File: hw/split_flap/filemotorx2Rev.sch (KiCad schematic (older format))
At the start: 4 parts, among them J13 Conn_01x05, J14 Conn_01x05, U7 PCF8574, U8 ULN2803A

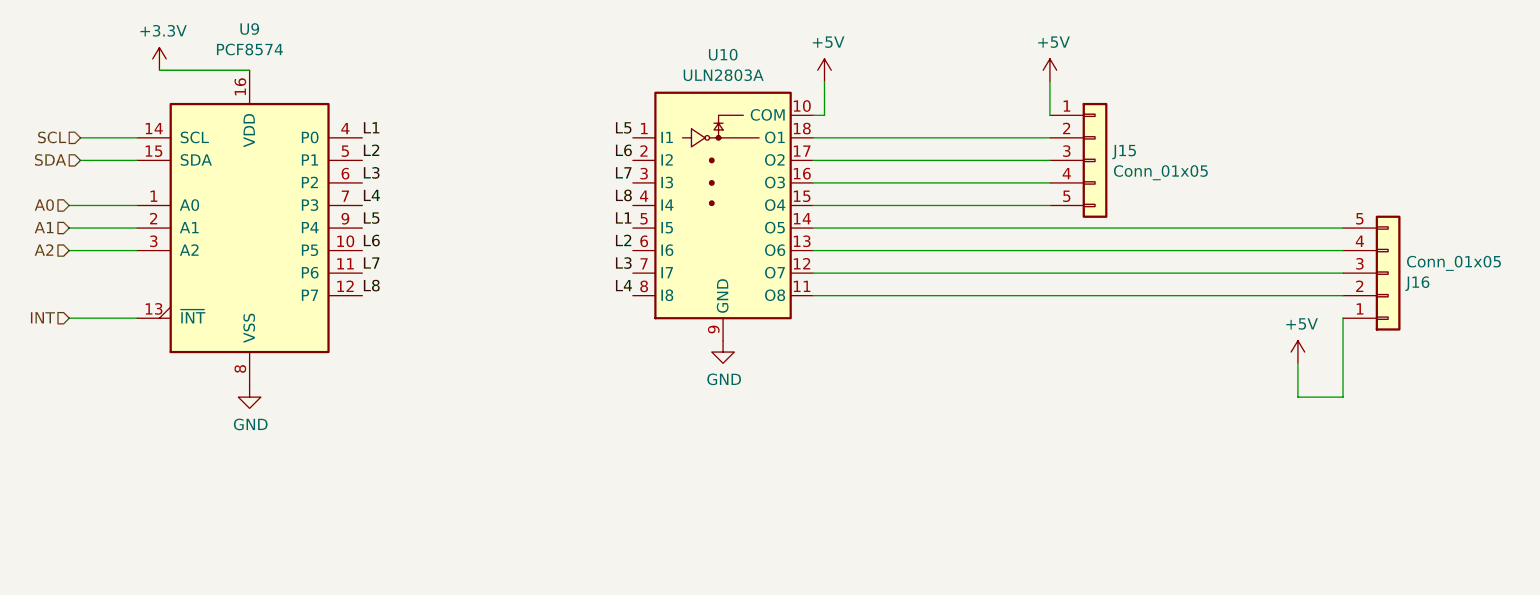
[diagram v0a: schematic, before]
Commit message: Reroute full PCB
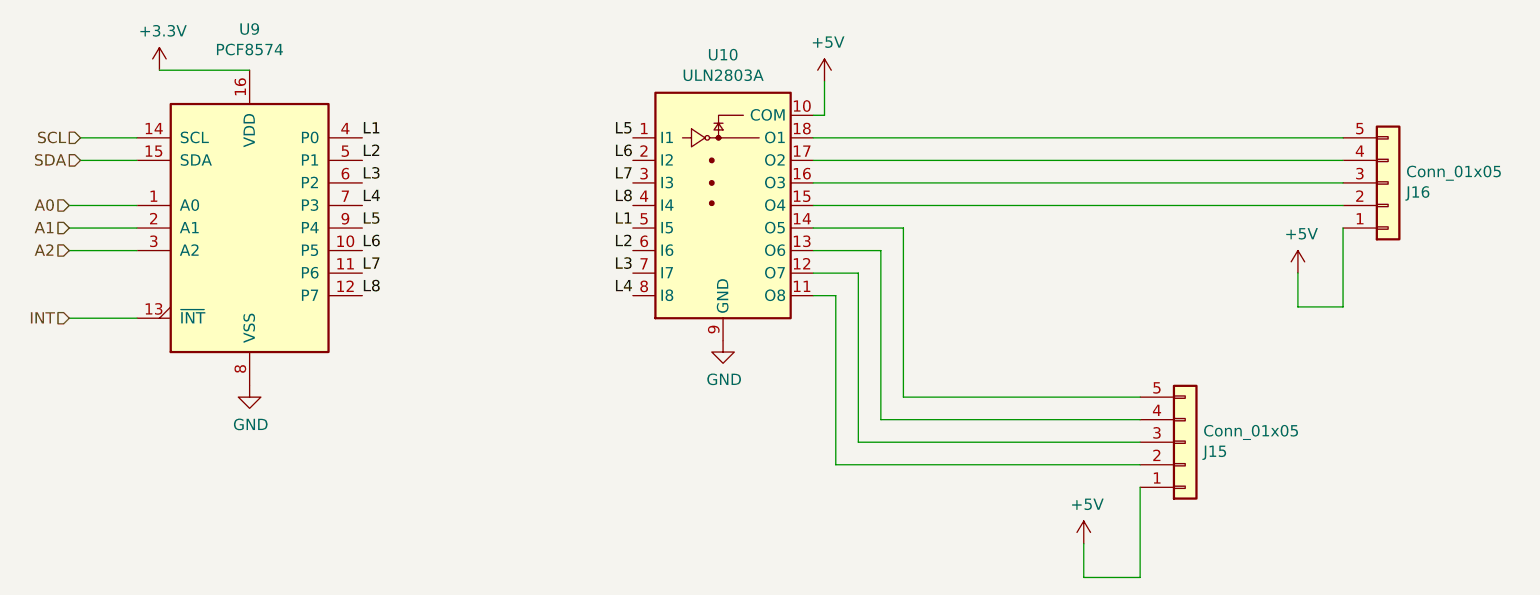
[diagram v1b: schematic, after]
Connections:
- net at J14.2 (Pin_2): now also U8.15 (O4); no longer U8.11 (O8)
- net at J14.3 (Pin_3): now also U8.16 (O3); no longer U8.12 (O7)
- net at J14.4 (Pin_4): now also U8.17 (O2); no longer U8.13 (O6)
- net at J14.5 (Pin_5): now also U8.18 (O1); no longer U8.14 (O5)
- net at J13.2 (Pin_2): now also U8.11 (O8); no longer U8.18 (O1)
- net at J13.3 (Pin_3): now also U8.12 (O7); no longer U8.17 (O2)
- net at J13.4 (Pin_4): now also U8.13 (O6); no longer U8.16 (O3)
- net at J13.5 (Pin_5): now also U8.14 (O5); no longer U8.15 (O4)
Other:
- moved on the sheet: J15, J16
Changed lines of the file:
@@
 $Descr A4 11693 8268
 encoding utf-8
-Sheet 4 7
+Sheet 5 7
 Title ""
 Date ""
@@
 	3400 3200 3000 3200
 Wire Wire Line
-	5900 4200 8250 4200
-Wire Wire Line
-	5900 4100 8250 4100
-Wire Wire Line
-	5900 4000 8250 4000
-Wire Wire Line
-	5900 3900 8250 3900
-Wire Wire Line
-	8050 4500 8050 4650
-$Comp
-L power:+5V #PWR?
-U 1 1 5DE20FD2
-P 8050 4500
-AR Path="/5DE20FD2" Ref="#PWR?"  Part="1"
-AR Path="/5E0CA2EA/5DE20FD2" Ref="#PWR?"  Part="1"
-AR Path="/5E1C4151/5DE20FD2" Ref="#PWR?"  Part="1"
-AR Path="/5E1CE3D2/5DE20FD2" Ref="#PWR?"  Part="1"
-AR Path="/5E1D4C2D/5DE20FD2" Ref="#PWR?"  Part="1"
-AR Path="/5E2ED868/5DE20FD2" Ref="#PWR?"  Part="1"
-AR Path="/5DE1D349/5DE20FD2" Ref="#PWR0121"  Part="1"
-AR Path="/5DE57FF9/5DE20FD2" Ref="#PWR0137"  Part="1"
-F 0 "#PWR0137" H 8050 4350 50  0001 C CNN
-F 1 "+5V" H 8065 4673 50  0000 C CNN
-F 2 "" H 8050 4500 50  0001 C CNN
-F 3 "" H 8050 4500 50  0001 C CNN
-	1    8050 4500
-	1    0    0    -1
-$EndComp
-$Comp
-L Connector_Generic:Conn_01x05 J?
-U 1 1 5DE20FD8
-P 8450 4100
-AR Path="/5DE20FD8" Ref="J?"  Part="1"
-AR Path="/5E0CA2EA/5DE20FD8" Ref="J?"  Part="1"
-AR Path="/5E1C4151/5DE20FD8" Ref="J?"  Part="1"
-AR Path="/5E1CE3D2/5DE20FD8" Ref="J?"  Part="1"
-AR Path="/5E1D4C2D/5DE20FD8" Ref="J?"  Part="1"
-AR Path="/5E2ED868/5DE20FD8" Ref="J?"  Part="1"
-AR Path="/5DE1D349/5DE20FD8" Ref="J14"  Part="1"
-AR Path="/5DE57FF9/5DE20FD8" Ref="J16"  Part="1"
-F 0 "J16" H 8530 4142 50  0000 L CNN
-F 1 "Conn_01x05" H 8530 4051 50  0000 L CNN
-F 2 "Connector_JST:JST_XH_B5B-XH-A_1x05_P2.50mm_Vertical" H 8450 4100 50  0001 C CNN
-F 3 "~" H 8450 4100 50  0001 C CNN
-	1    8450 4100
-	1    0    0    1
-$EndComp
-Wire Wire Line
 	5950 3400 5900 3400
 Wire Wire Line
 	5950 3250 5950 3400
-Wire Wire Line
-	6950 3250 6950 3400
-$Comp
-L power:+5V #PWR?
-U 1 1 5DE20FE1
-P 6950 3250
-AR Path="/5DE20FE1" Ref="#PWR?"  Part="1"
-AR Path="/5E0CA2EA/5DE20FE1" Ref="#PWR?"  Part="1"
-AR Path="/5E1C4151/5DE20FE1" Ref="#PWR?"  Part="1"
-AR Path="/5E1CE3D2/5DE20FE1" Ref="#PWR?"  Part="1"
-AR Path="/5E1D4C2D/5DE20FE1" Ref="#PWR?"  Part="1"
-AR Path="/5E2ED868/5DE20FE1" Ref="#PWR?"  Part="1"
-AR Path="/5DE1D349/5DE20FE1" Ref="#PWR0124"  Part="1"
-AR Path="/5DE57FF9/5DE20FE1" Ref="#PWR0138"  Part="1"
-F 0 "#PWR0138" H 6950 3100 50  0001 C CNN
-F 1 "+5V" H 6965 3423 50  0000 C CNN
-F 2 "" H 6950 3250 50  0001 C CNN
-F 3 "" H 6950 3250 50  0001 C CNN
-	1    6950 3250
-	1    0    0    -1
-$EndComp
 $Comp
 L power:+5V #PWR?
@@
 $EndComp
 $Comp
-L Connector_Generic:Conn_01x05 J?
-U 1 1 5DE20FF9
-P 7150 3600
-AR Path="/5DE20FF9" Ref="J?"  Part="1"
-AR Path="/5E0CA2EA/5DE20FF9" Ref="J?"  Part="1"
-AR Path="/5E1C4151/5DE20FF9" Ref="J?"  Part="1"
-AR Path="/5E1CE3D2/5DE20FF9" Ref="J?"  Part="1"
-AR Path="/5E1D4C2D/5DE20FF9" Ref="J?"  Part="1"
-AR Path="/5E2ED868/5DE20FF9" Ref="J?"  Part="1"
-AR Path="/5DE1D349/5DE20FF9" Ref="J13"  Part="1"
-AR Path="/5DE57FF9/5DE20FF9" Ref="J15"  Part="1"
-F 0 "J15" H 7230 3642 50  0000 L CNN
-F 1 "Conn_01x05" H 7230 3551 50  0000 L CNN
-F 2 "Connector_JST:JST_XH_B5B-XH-A_1x05_P2.50mm_Vertical" H 7150 3600 50  0001 C CNN
-F 3 "~" H 7150 3600 50  0001 C CNN
-	1    7150 3600
-	1    0    0    -1
-$EndComp
-Wire Wire Line
-	6950 3800 5900 3800
-Wire Wire Line
-	5900 3700 6950 3700
-Wire Wire Line
-	6950 3600 5900 3600
-Wire Wire Line
-	5900 3500 6950 3500
-$Comp
 L Interface_Expansion:PCF8574 U?
 U 1 1 5DE21003
@@
 	1    0    0    -1
 $EndComp
-Wire Wire Line
-	8250 4300 8250 4650
-Wire Wire Line
-	8250 4650 8050 4650
 Text Label 3900 3500 0    50   ~ 0
 L1
@@
 Text Label 5100 3800 2    50   ~ 0
 L8
+Wire Wire Line
+	8250 4250 8050 4250
+Wire Wire Line
+	8250 3900 8250 4250
+$Comp
+L Connector_Generic:Conn_01x05 J?
+U 1 1 5DE20FD8
+P 8450 3700
+AR Path="/5DE20FD8" Ref="J?"  Part="1"
+AR Path="/5E0CA2EA/5DE20FD8" Ref="J?"  Part="1"
+AR Path="/5E1C4151/5DE20FD8" Ref="J?"  Part="1"
+AR Path="/5E1CE3D2/5DE20FD8" Ref="J?"  Part="1"
+AR Path="/5E1D4C2D/5DE20FD8" Ref="J?"  Part="1"
+AR Path="/5E2ED868/5DE20FD8" Ref="J?"  Part="1"
+AR Path="/5DE1D349/5DE20FD8" Ref="J14"  Part="1"
+AR Path="/5DE57FF9/5DE20FD8" Ref="J16"  Part="1"
+F 0 "J16" H 8530 3742 50  0000 L CNN
+F 1 "Conn_01x05" H 8530 3651 50  0000 L CNN
+F 2 "Connector_JST:JST_XH_B5B-XH-A_1x05_P2.50mm_Vertical" H 8450 3700 50  0001 C CNN
+F 3 "~" H 8450 3700 50  0001 C CNN
+	1    8450 3700
+	1    0    0    1
+$EndComp
+$Comp
+L power:+5V #PWR?
+U 1 1 5DE20FD2
+P 8050 4100
+AR Path="/5DE20FD2" Ref="#PWR?"  Part="1"
+AR Path="/5E0CA2EA/5DE20FD2" Ref="#PWR?"  Part="1"
+AR Path="/5E1C4151/5DE20FD2" Ref="#PWR?"  Part="1"
+AR Path="/5E1CE3D2/5DE20FD2" Ref="#PWR?"  Part="1"
+AR Path="/5E1D4C2D/5DE20FD2" Ref="#PWR?"  Part="1"
+AR Path="/5E2ED868/5DE20FD2" Ref="#PWR?"  Part="1"
+AR Path="/5DE1D349/5DE20FD2" Ref="#PWR0121"  Part="1"
+AR Path="/5DE57FF9/5DE20FD2" Ref="#PWR0137"  Part="1"
+F 0 "#PWR0137" H 8050 3950 50  0001 C CNN
+F 1 "+5V" H 8065 4273 50  0000 C CNN
+F 2 "" H 8050 4100 50  0001 C CNN
+F 3 "" H 8050 4100 50  0001 C CNN
+	1    8050 4100
+	1    0    0    -1
+$EndComp
+Wire Wire Line
+	8050 4100 8050 4250
+Wire Wire Line
+	5900 3500 8250 3500
+Wire Wire Line
+	5900 3600 8250 3600
+Wire Wire Line
+	5900 3700 8250 3700
+Wire Wire Line
+	5900 3800 8250 3800
+Wire Wire Line
+	6300 4650 7350 4650
+$Comp
+L Connector_Generic:Conn_01x05 J?
+U 1 1 5DE20FF9
+P 7550 4850
+AR Path="/5DE20FF9" Ref="J?"  Part="1"
+AR Path="/5E0CA2EA/5DE20FF9" Ref="J?"  Part="1"
+AR Path="/5E1C4151/5DE20FF9" Ref="J?"  Part="1"
+AR Path="/5E1CE3D2/5DE20FF9" Ref="J?"  Part="1"
+AR Path="/5E1D4C2D/5DE20FF9" Ref="J?"  Part="1"
+AR Path="/5E2ED868/5DE20FF9" Ref="J?"  Part="1"
+AR Path="/5DE1D349/5DE20FF9" Ref="J13"  Part="1"
+AR Path="/5DE57FF9/5DE20FF9" Ref="J15"  Part="1"
+F 0 "J15" H 7630 4892 50  0000 L CNN
+F 1 "Conn_01x05" H 7630 4801 50  0000 L CNN
+F 2 "Connector_JST:JST_XH_B5B-XH-A_1x05_P2.50mm_Vertical" H 7550 4850 50  0001 C CNN
+F 3 "~" H 7550 4850 50  0001 C CNN
+	1    7550 4850
+	1    0    0    1
+$EndComp
+Wire Wire Line
+	5900 3900 6300 3900
+Wire Wire Line
+	6300 3900 6300 4650
+Wire Wire Line
+	5900 4000 6200 4000
+Wire Wire Line
+	6200 4000 6200 4750
+Wire Wire Line
+	6200 4750 7350 4750
+Wire Wire Line
+	5900 4100 6100 4100
+Wire Wire Line
+	6100 4100 6100 4850
+Wire Wire Line
+	6100 4850 7350 4850
+Wire Wire Line
+	5900 4200 6000 4200
+Wire Wire Line
+	6000 4200 6000 4950
+Wire Wire Line
+	6000 4950 7350 4950
+$Comp
+L power:+5V #PWR?
+U 1 1 5DE2DF9C
+P 7100 5300
+AR Path="/5DE2DF9C" Ref="#PWR?"  Part="1"
+AR Path="/5E0CA2EA/5DE2DF9C" Ref="#PWR?"  Part="1"
+AR Path="/5E1C4151/5DE2DF9C" Ref="#PWR?"  Part="1"
+AR Path="/5E1CE3D2/5DE2DF9C" Ref="#PWR?"  Part="1"
+AR Path="/5E1D4C2D/5DE2DF9C" Ref="#PWR?"  Part="1"
+AR Path="/5E2ED868/5DE2DF9C" Ref="#PWR?"  Part="1"
+AR Path="/5DE1D349/5DE2DF9C" Ref="#PWR0124"  Part="1"
+AR Path="/5DE57FF9/5DE2DF9C" Ref="#PWR0138"  Part="1"
+F 0 "#PWR0138" H 7100 5150 50  0001 C CNN
+F 1 "+5V" H 7115 5473 50  0000 C CNN
+F 2 "" H 7100 5300 50  0001 C CNN
+F 3 "" H 7100 5300 50  0001 C CNN
+	1    7100 5300
+	1    0    0    -1
+$EndComp
+Wire Wire Line
+	7100 5300 7100 5450
+Wire Wire Line
+	7350 5050 7350 5450
+Wire Wire Line
+	7100 5450 7350 5450
 $EndSCHEMATC

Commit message: hw: Route pcb completely
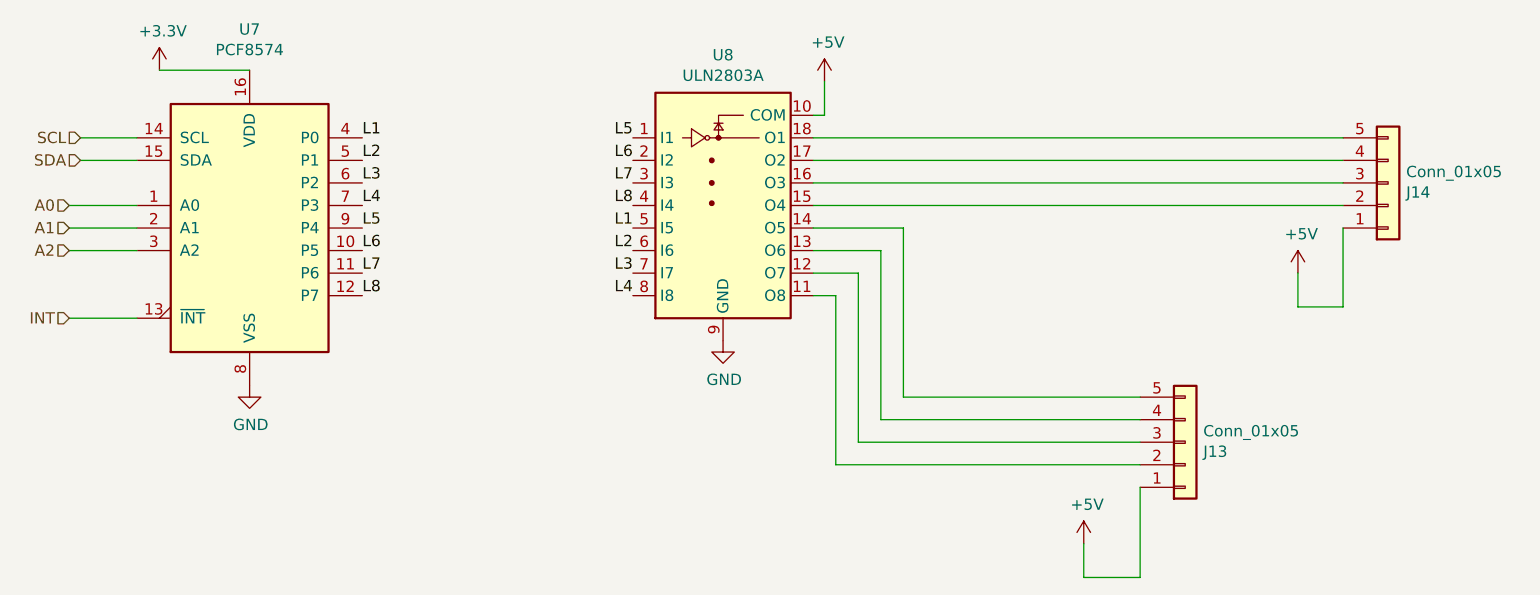
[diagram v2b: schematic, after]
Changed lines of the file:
@@
 $Descr A4 11693 8268
 encoding utf-8
-Sheet 5 7
+Sheet 4 7
 Title ""
 Date ""
@@
 AR Path="/5DE1D349/5DE21003" Ref="U7"  Part="1"
 AR Path="/5DE57FF9/5DE21003" Ref="U9"  Part="1"
-F 0 "U9" H 3400 4781 50  0000 C CNN
+F 0 "U7" H 3400 4781 50  0000 C CNN
 F 1 "PCF8574" H 3400 4690 50  0000 C CNN
 F 2 "Package_SO:SOIC-16W_7.5x10.3mm_P1.27mm" H 3400 3900 50  0001 C CNN
@@
 AR Path="/5DE1D349/5DE21009" Ref="U8"  Part="1"
 AR Path="/5DE57FF9/5DE21009" Ref="U10"  Part="1"
-F 0 "U10" H 5500 4267 50  0000 C CNN
+F 0 "U8" H 5500 4267 50  0000 C CNN
 F 1 "ULN2803A" H 5500 4176 50  0000 C CNN
 F 2 "Package_SO:SOP-18_7x12.5mm_P1.27mm" H 5550 3050 50  0001 L CNN
@@
 AR Path="/5DE1D349/5DE20FD8" Ref="J14"  Part="1"
 AR Path="/5DE57FF9/5DE20FD8" Ref="J16"  Part="1"
-F 0 "J16" H 8530 3742 50  0000 L CNN
+F 0 "J14" H 8530 3742 50  0000 L CNN
 F 1 "Conn_01x05" H 8530 3651 50  0000 L CNN
 F 2 "Connector_JST:JST_XH_B5B-XH-A_1x05_P2.50mm_Vertical" H 8450 3700 50  0001 C CNN
@@
 AR Path="/5DE1D349/5DE20FF9" Ref="J13"  Part="1"
 AR Path="/5DE57FF9/5DE20FF9" Ref="J15"  Part="1"
-F 0 "J15" H 7630 4892 50  0000 L CNN
+F 0 "J13" H 7630 4892 50  0000 L CNN
 F 1 "Conn_01x05" H 7630 4801 50  0000 L CNN
 F 2 "Connector_JST:JST_XH_B5B-XH-A_1x05_P2.50mm_Vertical" H 7550 4850 50  0001 C CNN
